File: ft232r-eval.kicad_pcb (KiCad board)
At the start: 2 copper layers, 25 x 53 mm, 15 parts, among them J1 USB_A, J2 FTDI, J3 JST, SW1 VIO_SEL, U1 FT232RL

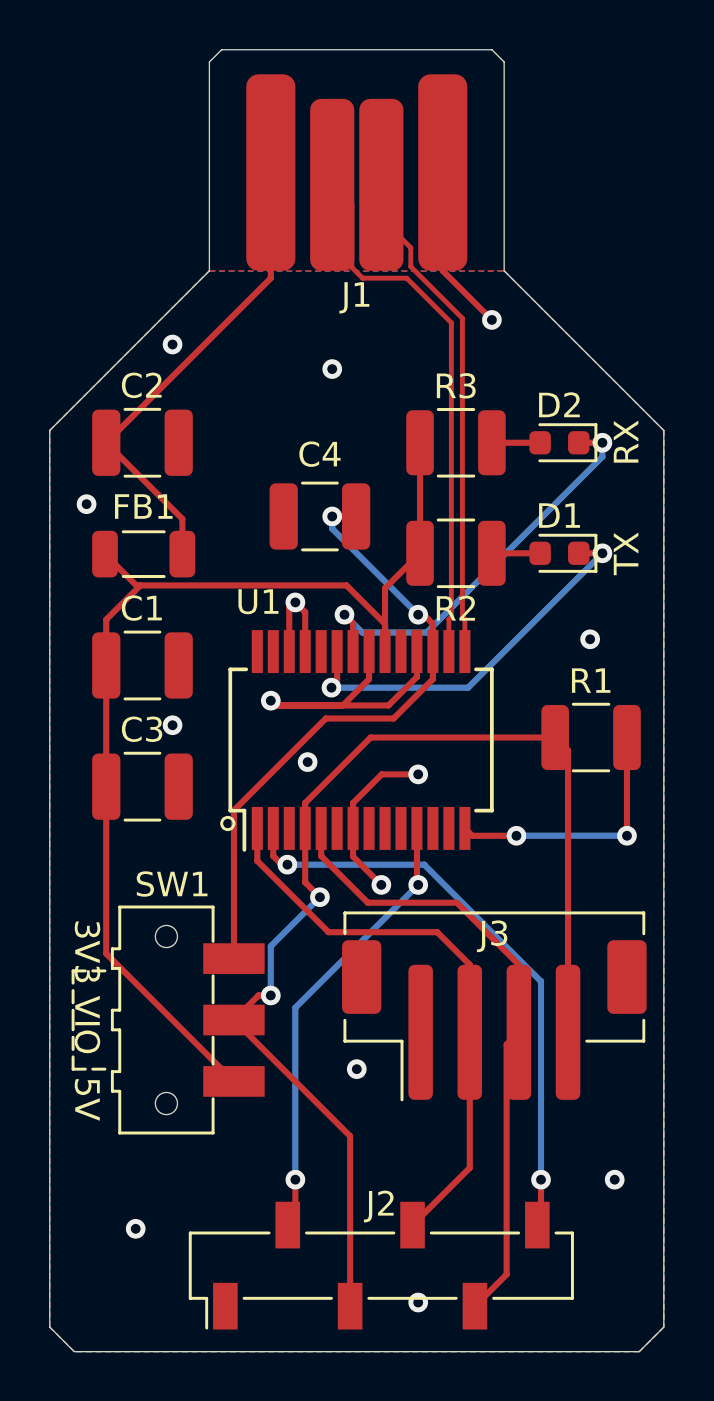
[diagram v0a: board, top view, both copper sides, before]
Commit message: Fix FTDI header footprint
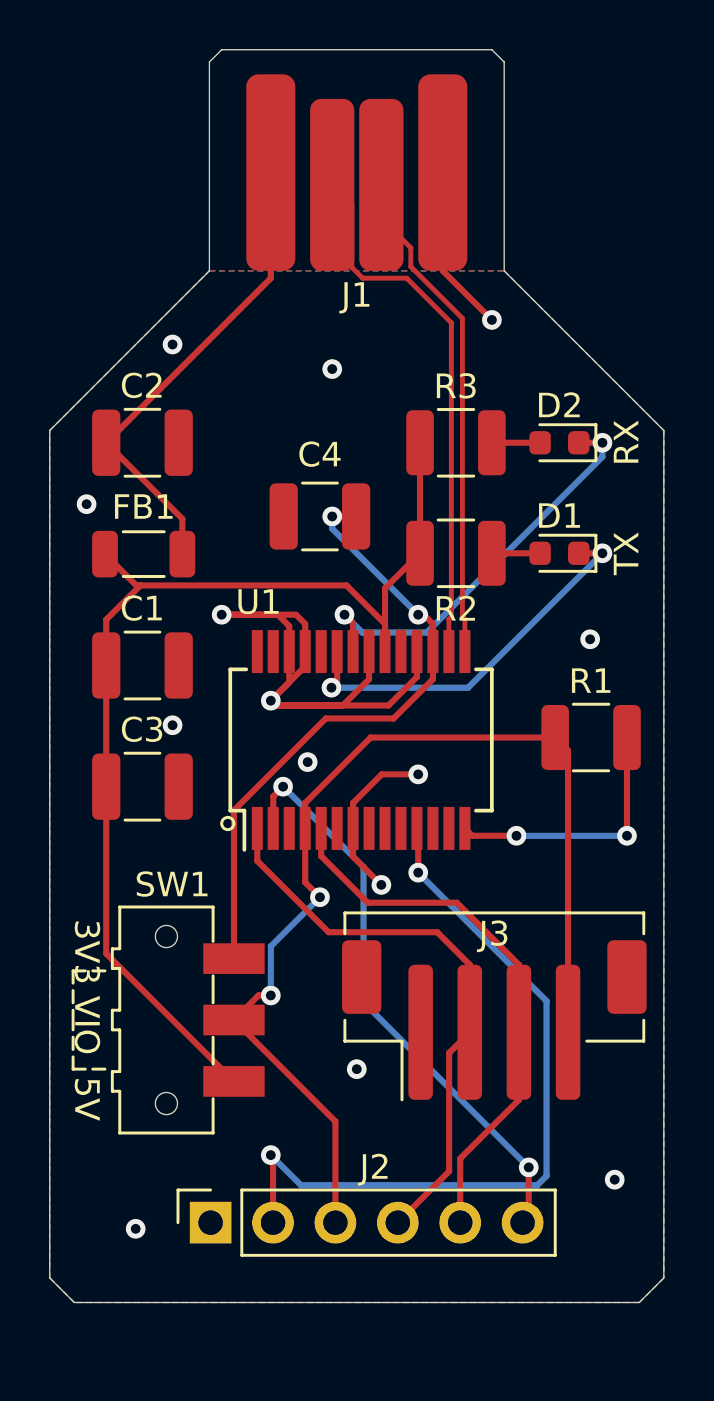
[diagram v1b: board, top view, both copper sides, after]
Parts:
- J2: footprint Connector_PinSocket_2.54mm:PinSocket_1x06_P2.54mm_Vertical_SMD_Pin1Left -> Connector_PinSocket_2.54mm:PinSocket_1x06_P2.54mm_Vertical
- moved J2 7.17 mm to (139.6, 101.8)
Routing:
- net /CTS: track 18.4 -> 31.0 mm
- net GND: track 31.0 -> 40.2 mm, vias 15 -> 14
- net /VIO: track 47.9 -> 44.3 mm
- net /RXD: track 25.6 -> 22.5 mm
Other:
- board size 25 x 53 mm -> 25 x 51 mm

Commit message: Add labels for J2 and J3 pins
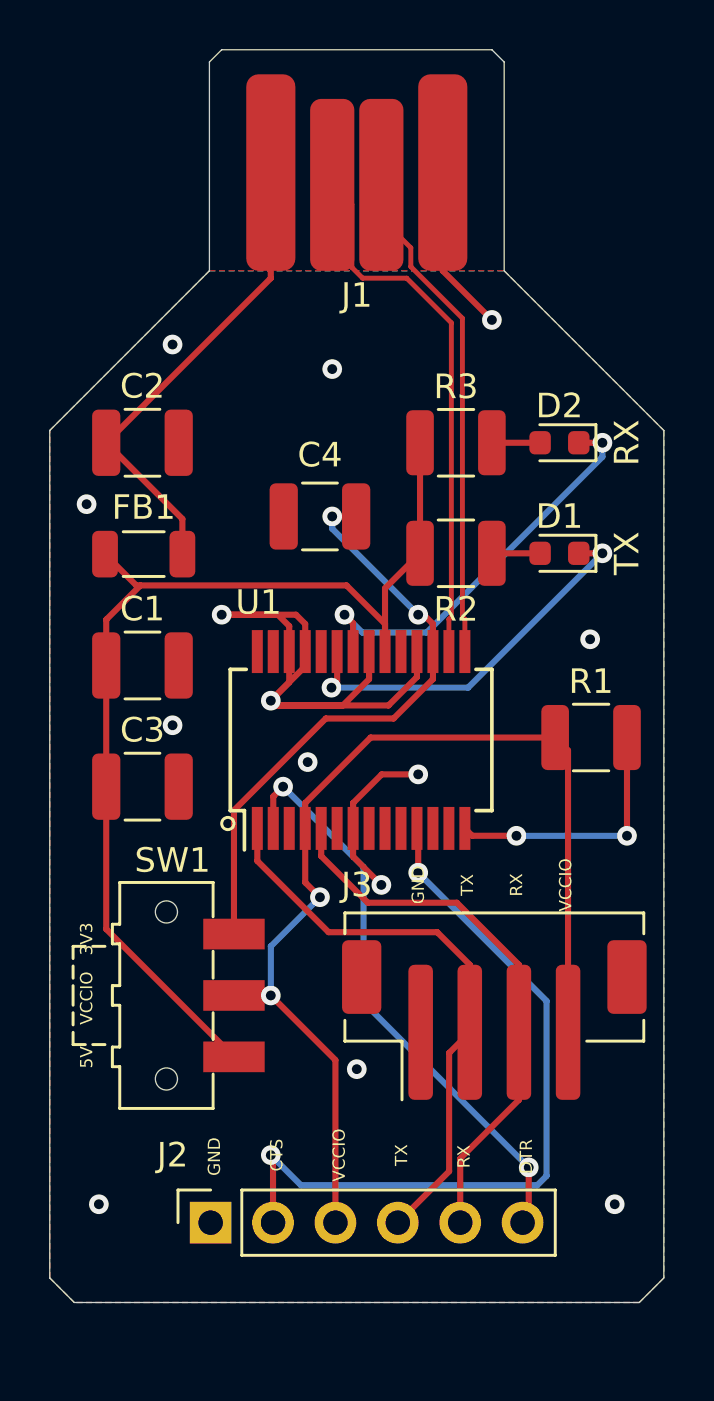
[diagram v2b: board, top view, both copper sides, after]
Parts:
- moved SW1 1.00 mm to (137.8, 92.5)
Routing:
- net VCC: track 45.7 -> 44.7 mm
- net +3V3: track 25.8 -> 24.8 mm
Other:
- board text added: "5V VCCIO 3V3"
- board text added: "CTS"
- board text added: "DTR"
- board text added: "FT232R Evaluation Board v2 C. Keller 2021-04-02"
- board text added: "GND"
- board text added: "RX"
- board text added: "TX"
- board text added: "VCCIO"
- board text removed: "3V3 VIO 5V"
- board text removed: "FT232R Evaluation Board v1 C. Keller 2021-03-24"
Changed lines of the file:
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@@
-(kicad_pcb (version 20171130) (host pcbnew 5.1.9)
+(kicad_pcb (version 20171130) (host pcbnew "(5.1.9-0-10_14)")
   (general
     (thickness 1.6)
-    (drawings 15)
+    (drawings 25)
     (tracks 159)
     (zones 0)
@@
   )
   (page A4)
+  (title_block
+    (title "FT232R Evaluation Board")
+    (date 2021-04-02)
+    (rev 2)
+    (company "Chris Keller")
+  )
   (layers
     (0 F.Cu signal)
@@
     (descr "Through hole straight socket strip, 1x06, 2.54mm pitch, single row (from Kicad 4.0.7), script generated")
     (tags "Through hole socket strip THT 1x06 2.54mm single row")
-    (fp_text reference J2 (at 2.25 6.7 180) (layer F.SilkS)
+    (fp_text reference J2 (at 2.75 -1.55 180) (layer F.SilkS)
       (effects (font (size 1 1) (thickness 0.15)))
     )
     (fp_text value FTDI (at 0 15.47 90) (layer F.Fab)
-      (effects (font (size 1 1) (thickness 0.15)))
-    )
-    (fp_text user %R (at 0 6.35) (layer F.Fab)
       (effects (font (size 1 1) (thickness 0.15)))
     )
@@
     (fp_line (start 1.75 14.45) (end -1.8 14.45) (layer F.CrtYd) (width 0.05))
     (fp_line (start -1.8 14.45) (end -1.8 -1.8) (layer F.CrtYd) (width 0.05))
+    (fp_text user %R (at 0 6.35) (layer F.Fab)
+      (effects (font (size 1 1) (thickness 0.15)))
+    )
     (pad 6 thru_hole oval (at 0 12.7 90) (size 1.7 1.7) (drill 1) (layers *.Cu *.Mask)
       (net 11 /DTR))
@@
   )
   (module Button_Switch_SMD:SW_SPDT_CK-JS102011SAQN (layer F.Cu)
-    (at 137.75 93.5 270)
+    (at 137.75 92.5 270)
     (descr "Sub-miniature slide switch, right-angle, http://www.ckswitches.com/media/1422/js.pdf")
     (tags "switch spdt")
@@
     (tags "connector JST PH side entry")
     (attr smd)
-    (fp_text reference J3 (at 0 -3.5) (layer F.SilkS)
+    (fp_text reference J3 (at -5.6 -5.5) (layer F.SilkS)
       (effects (font (size 1 1) (thickness 0.15)))
     )
@@
       (rotate (xyz 0 0 0))
     )
+    (model ${KIPRJMOD}/Libraries/B4B-PH-SM4-TBT_LF__SN_.stp
+      (offset (xyz 0 1.75 0))
+      (scale (xyz 1 1 1))
+      (rotate (xyz 0 0 0))
+    )
   )
   (module Inductor_SMD:L_1206_3216Metric (layer F.Cu)
@@
     )
   )
+  (gr_text "5V    VCCIO   3V3" (at 134.5 92.5 90) (layer F.SilkS)
+    (effects (font (size 0.5 0.5) (thickness 0.125)))
+  )
+  (gr_text CTS (at 142.24 99 90) (layer F.SilkS)
+    (effects (font (size 0.5 0.5) (thickness 0.125)))
+  )
+  (gr_text DTR (at 152.4 99.06 90) (layer F.SilkS)
+    (effects (font (size 0.5 0.5) (thickness 0.125)))
+  )
+  (gr_text RX (at 149.86 99.06 90) (layer F.SilkS)
+    (effects (font (size 0.5 0.5) (thickness 0.125)))
+  )
+  (gr_text TX (at 147.32 99 90) (layer F.SilkS)
+    (effects (font (size 0.5 0.5) (thickness 0.125)))
+  )
+  (gr_text GND (at 139.7 99.06 90) (layer F.SilkS)
+    (effects (font (size 0.5 0.5) (thickness 0.125)))
+  )
+  (gr_text VCCIO (at 144.78 99 90) (layer F.SilkS)
+    (effects (font (size 0.5 0.5) (thickness 0.125)))
+  )
+  (gr_text GND (at 148 88 90) (layer F.SilkS)
+    (effects (font (size 0.5 0.5) (thickness 0.125)))
+  )
+  (gr_text TX (at 150 88 90) (layer F.SilkS)
+    (effects (font (size 0.5 0.5) (thickness 0.125)))
+  )
+  (gr_text RX (at 152 88 90) (layer F.SilkS)
+    (effects (font (size 0.5 0.5) (thickness 0.125)))
+  )
+  (gr_text VCCIO (at 154 88 90) (layer F.SilkS)
+    (effects (font (size 0.5 0.5) (thickness 0.125)))
+  )
   (gr_circle (center 140.25 85.5) (end 140.5 85.5) (layer F.SilkS) (width 0.12))
-  (gr_text "3V3 VIO  5V" (at 134.5 93.5 -90) (layer F.SilkS)
-    (effects (font (size 1 1) (thickness 0.15)))
-  )
-  (gr_text "FT232R Evaluation Board v1\nC. Keller 2021-03-24" (at 142.25 78.25 90) (layer B.SilkS)
+  (gr_text "FT232R Evaluation Board v2\nC. Keller 2021-04-02" (at 142.25 78.25 90) (layer B.SilkS)
     (effects (font (size 1 1) (thickness 0.15)) (justify mirror))
   )
@@
   (via (at 143.5 83) (size 0.8) (drill 0.4) (layers F.Cu B.Cu) (net 1))
   (via (at 155 78) (size 0.8) (drill 0.4) (layers F.Cu B.Cu) (net 1))
-  (via (at 136.5 102) (size 0.8) (drill 0.4) (layers F.Cu B.Cu) (net 1))
+  (via (at 135 101) (size 0.8) (drill 0.4) (layers F.Cu B.Cu) (net 1))
   (via (at 145.5 95.5) (size 0.8) (drill 0.4) (layers F.Cu B.Cu) (net 1))
-  (via (at 156 100) (size 0.8) (drill 0.4) (layers F.Cu B.Cu) (net 1))
+  (via (at 156 101) (size 0.8) (drill 0.4) (layers F.Cu B.Cu) (net 1))
   (segment (start 146.514998 83.5) (end 148 83.5) (width 0.25) (layer F.Cu) (net 1))
   (segment (start 145.35 84.664998) (end 146.514998 83.5) (width 0.25) (layer F.Cu) (net 1))
@@
   (segment (start 145.083343 75.808343) (end 136.691657 75.808343) (width 0.25) (layer F.Cu) (net 2))
   (segment (start 135.3 84) (end 135.3 79.066666) (width 0.25) (layer F.Cu) (net 2))
-  (segment (start 135.3 90.8) (end 140.5 96) (width 0.25) (layer F.Cu) (net 2))
-  (segment (start 135.3 84) (end 135.3 90.8) (width 0.25) (layer F.Cu) (net 2))
+  (segment (start 135.3 89.8) (end 140.5 95) (width 0.25) (layer F.Cu) (net 2))
+  (segment (start 135.3 84) (end 135.3 89.8) (width 0.25) (layer F.Cu) (net 2))
   (segment (start 138.4 73.1) (end 135.3 70) (width 0.25) (layer F.Cu) (net 3))
   (segment (start 138.4 74.533333) (end 138.4 73.1) (width 0.25) (layer F.Cu) (net 3))
@@
   (segment (start 144.5 73) (end 145.475 73) (width 0.25) (layer F.Cu) (net 4))
   (segment (start 144.239997 81.225001) (end 140.5 84.964998) (width 0.25) (layer F.Cu) (net 4))
-  (segment (start 140.5 84.964998) (end 140.5 91) (width 0.25) (layer F.Cu) (net 4))
   (segment (start 146.999999 81.225001) (end 144.239997 81.225001) (width 0.25) (layer F.Cu) (net 4))
   (segment (start 148.6 79.625) (end 146.999999 81.225001) (width 0.25) (layer F.Cu) (net 4))
   (segment (start 148.6 78.5) (end 148.6 79.625) (width 0.25) (layer F.Cu) (net 4))
+  (segment (start 140.5 90) (end 140.5 84.964998) (width 0.25) (layer F.Cu) (net 4))
   (segment (start 151 74.5) (end 152.9625 74.5) (width 0.25) (layer F.Cu) (net 5))
   (via (at 144.469846 79.969846) (size 0.8) (drill 0.4) (layers F.Cu B.Cu) (net 6))
@@
   (segment (start 142 90.5) (end 142 92.5) (width 0.25) (layer B.Cu) (net 15))
   (segment (start 144 88.5) (end 142 90.5) (width 0.25) (layer B.Cu) (net 15))
-  (segment (start 141.5 92.5) (end 140.5 93.5) (width 0.25) (layer F.Cu) (net 15))
   (segment (start 142 92.5) (end 141.5 92.5) (width 0.25) (layer F.Cu) (net 15))
-  (segment (start 144.63 97.63) (end 140.5 93.5) (width 0.25) (layer F.Cu) (net 15))
-  (segment (start 144.63 101.75) (end 144.63 97.63) (width 0.25) (layer F.Cu) (net 15))
+  (segment (start 142 92.5) (end 140.5 92.5) (width 0.25) (layer F.Cu) (net 15))
+  (segment (start 144.63 95.13) (end 144.63 101.75) (width 0.25) (layer F.Cu) (net 15))
+  (segment (start 142 92.5) (end 144.63 95.13) (width 0.25) (layer F.Cu) (net 15))
   (via (at 156.5 86) (size 0.8) (drill 0.4) (layers F.Cu B.Cu) (net 16))
   (segment (start 156.5 82) (end 156.5 86) (width 0.25) (layer F.Cu) (net 16))

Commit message: Thicker traces and fix 3D render
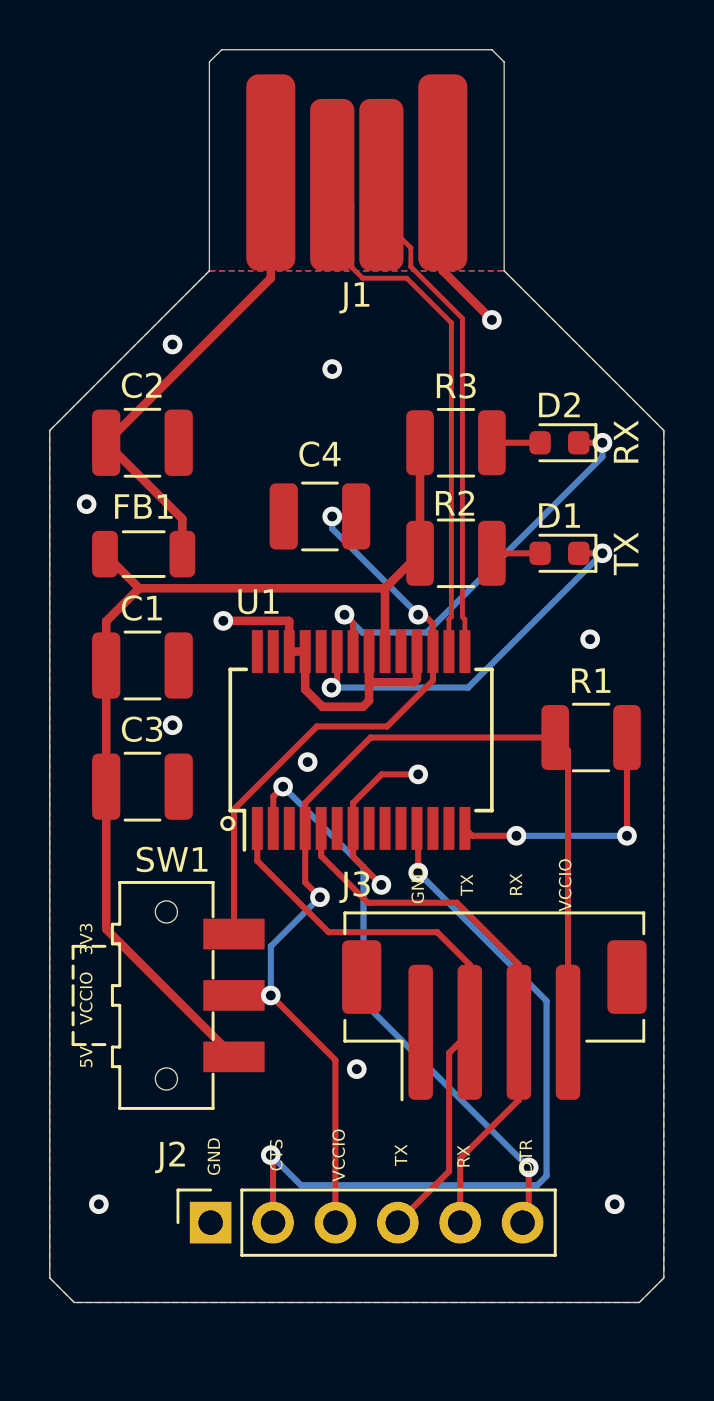
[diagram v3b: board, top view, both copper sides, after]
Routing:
- net GND: track 40.2 -> 29.2 mm, vias 14 -> 13
- net VCC: track 44.7 -> 42.9 mm
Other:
- net class Power added: clearance 0.2, trace_width 0.35, via_dia 0.8, via_drill 0.4
- board text added: "FT232R Evaluation Board v2 C. Keller 2021-04-05"
- board text removed: "FT232R Evaluation Board v2 C. Keller 2021-04-02"

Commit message: Add LED directional arrows
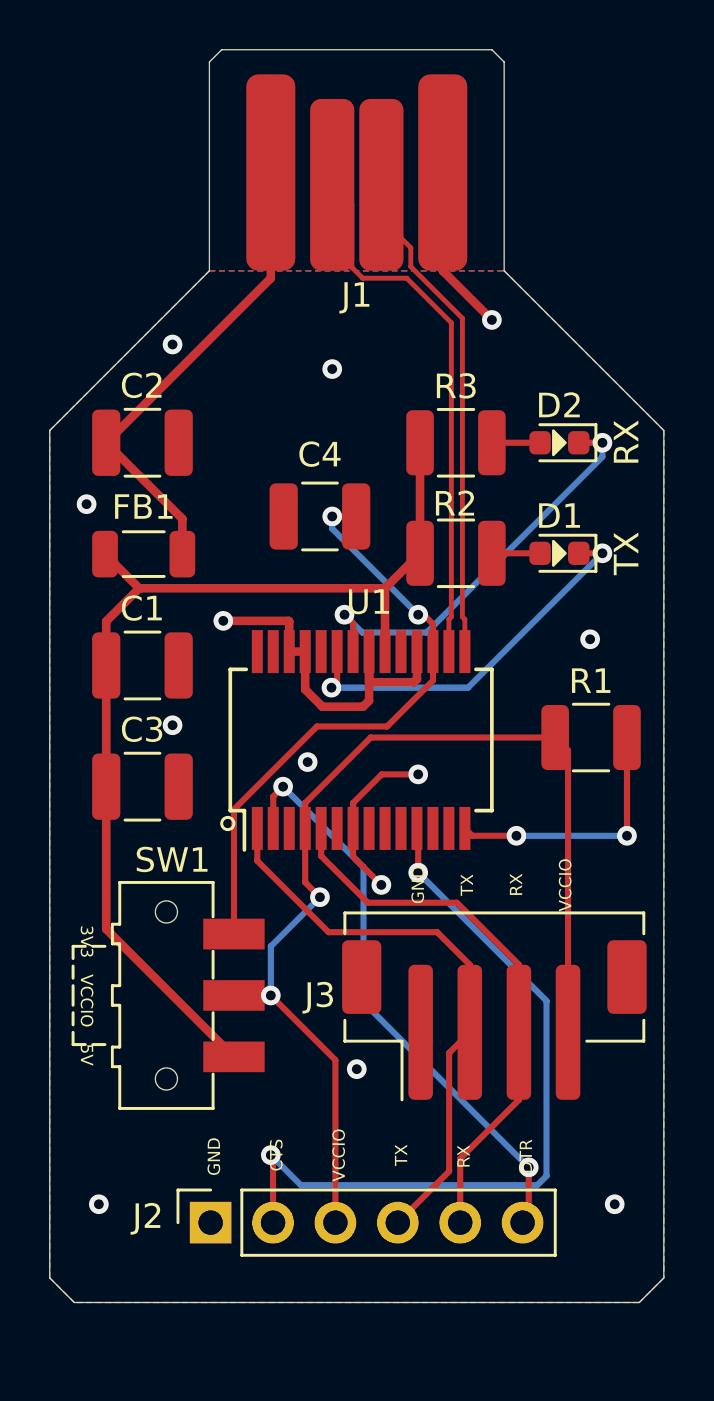
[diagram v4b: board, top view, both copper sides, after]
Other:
- board text added: "3V3 VCCIO 5V"
- board text removed: "5V VCCIO 3V3"
